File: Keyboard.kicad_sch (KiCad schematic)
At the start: 12 parts, among them J1 SPI Display, U1 MCP23017_SO, U2 MCP23017_SO, U3 Seeeduino Xiao nRF52840

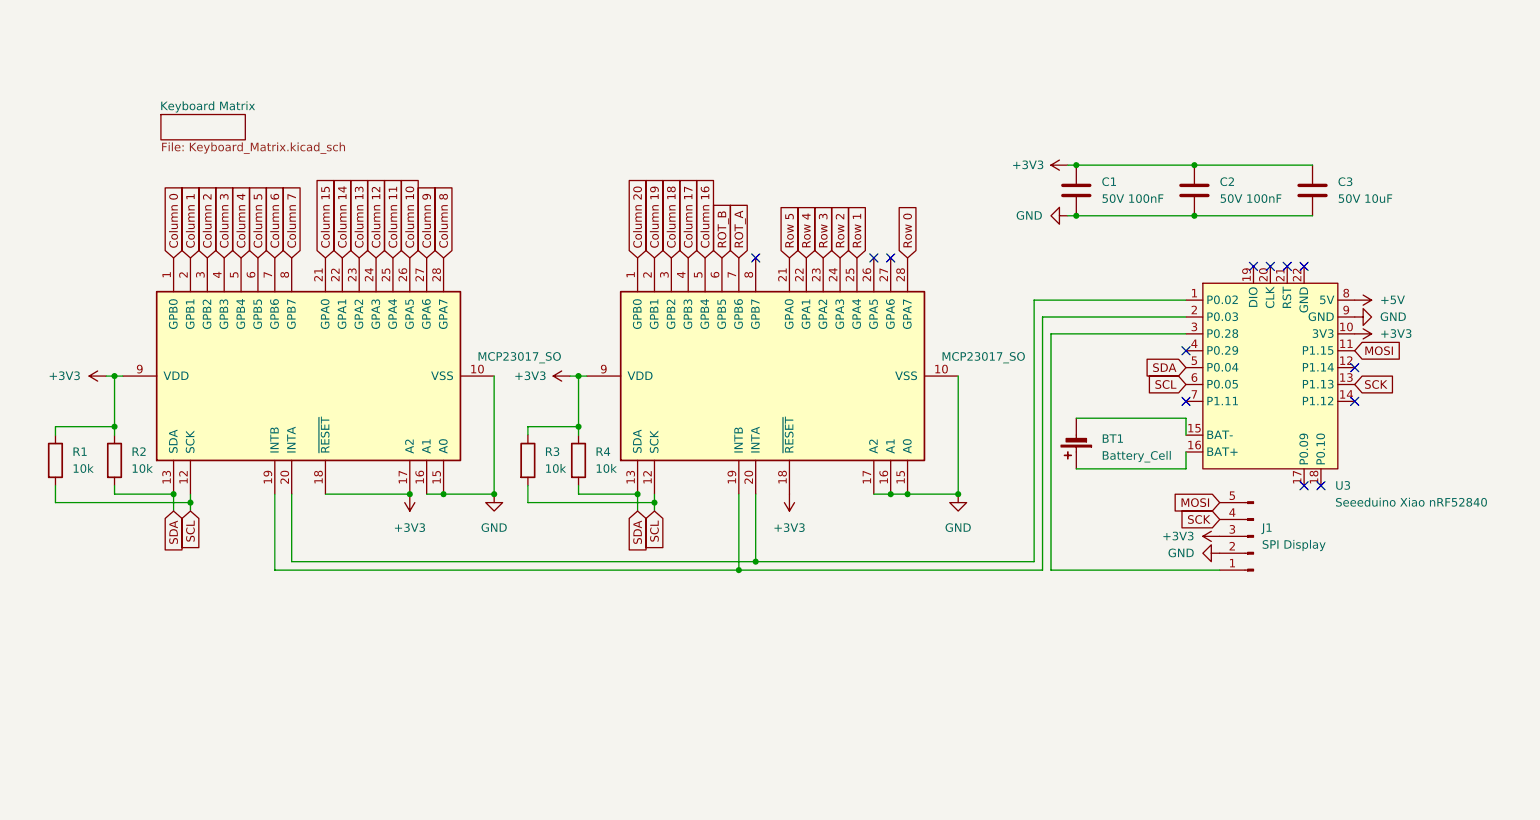
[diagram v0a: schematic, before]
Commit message: Replaced Rotary Encoder.
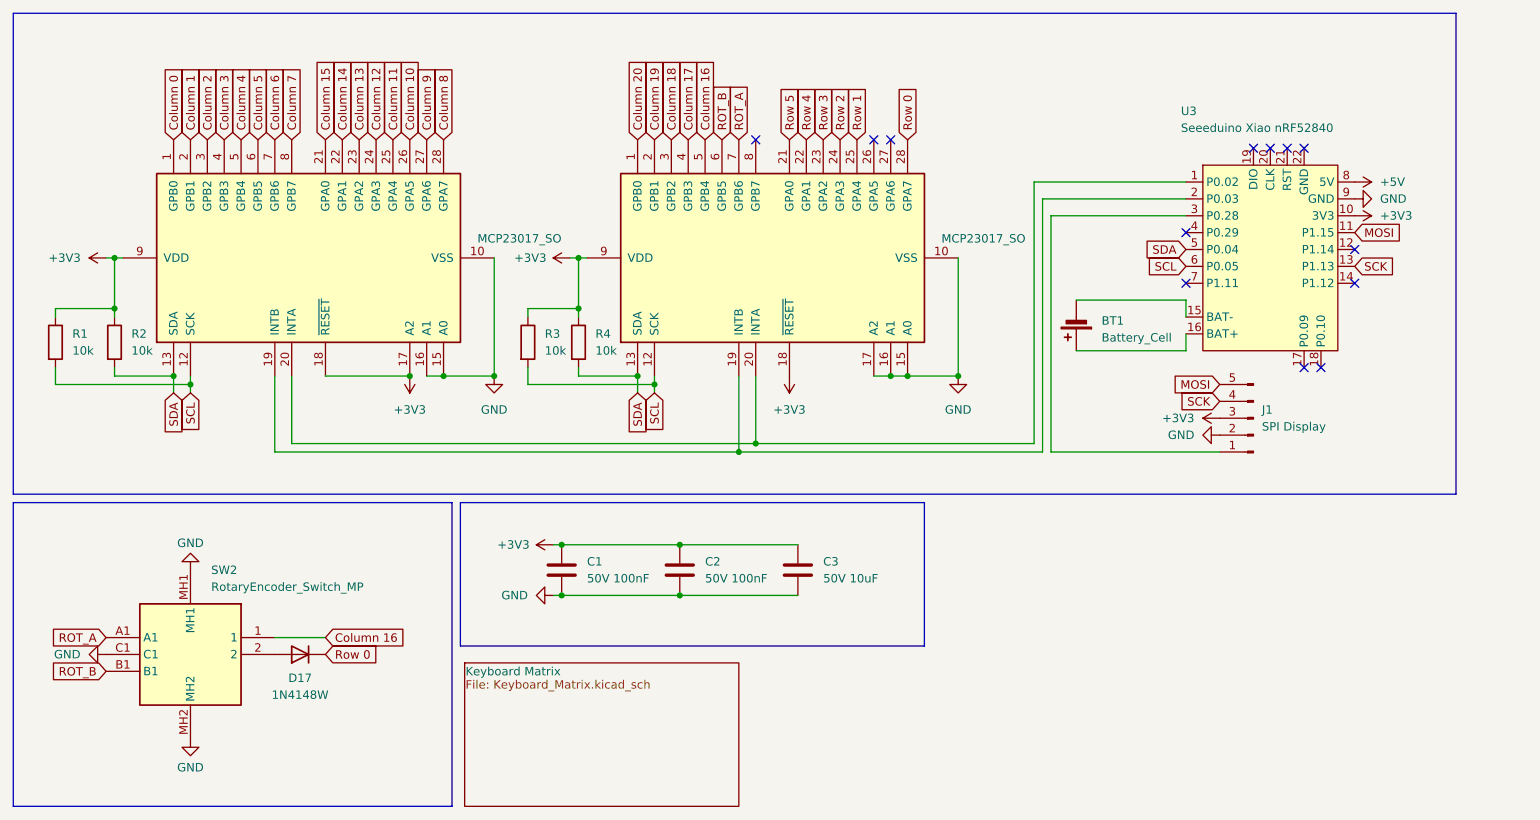
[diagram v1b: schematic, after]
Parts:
- added D17: 1N4148W, Diode_SMD:D_SOD-123, symbol Diode:1N4148W
- added SW2: RotaryEncoder_Switch_MP, SamacSys_Parts:PEC11L4115FS0020, symbol SamacSys_Parts:PEC11L-4115F-S0020
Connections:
- net Column 16: now also SW2.1
- net GND: now also SW2.C1, SW2.MH1, SW2.MH2
- net ROT_A: now also SW2.A1
- net ROT_B: now also SW2.B1
- net Row 0: now also D17.1 (K)
- new net: D17.2 (A), SW2.2
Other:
- moved on the sheet: BT1, C1, C2, C3, J1, R1, R2, R3, R4, U3

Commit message: Changed routing.
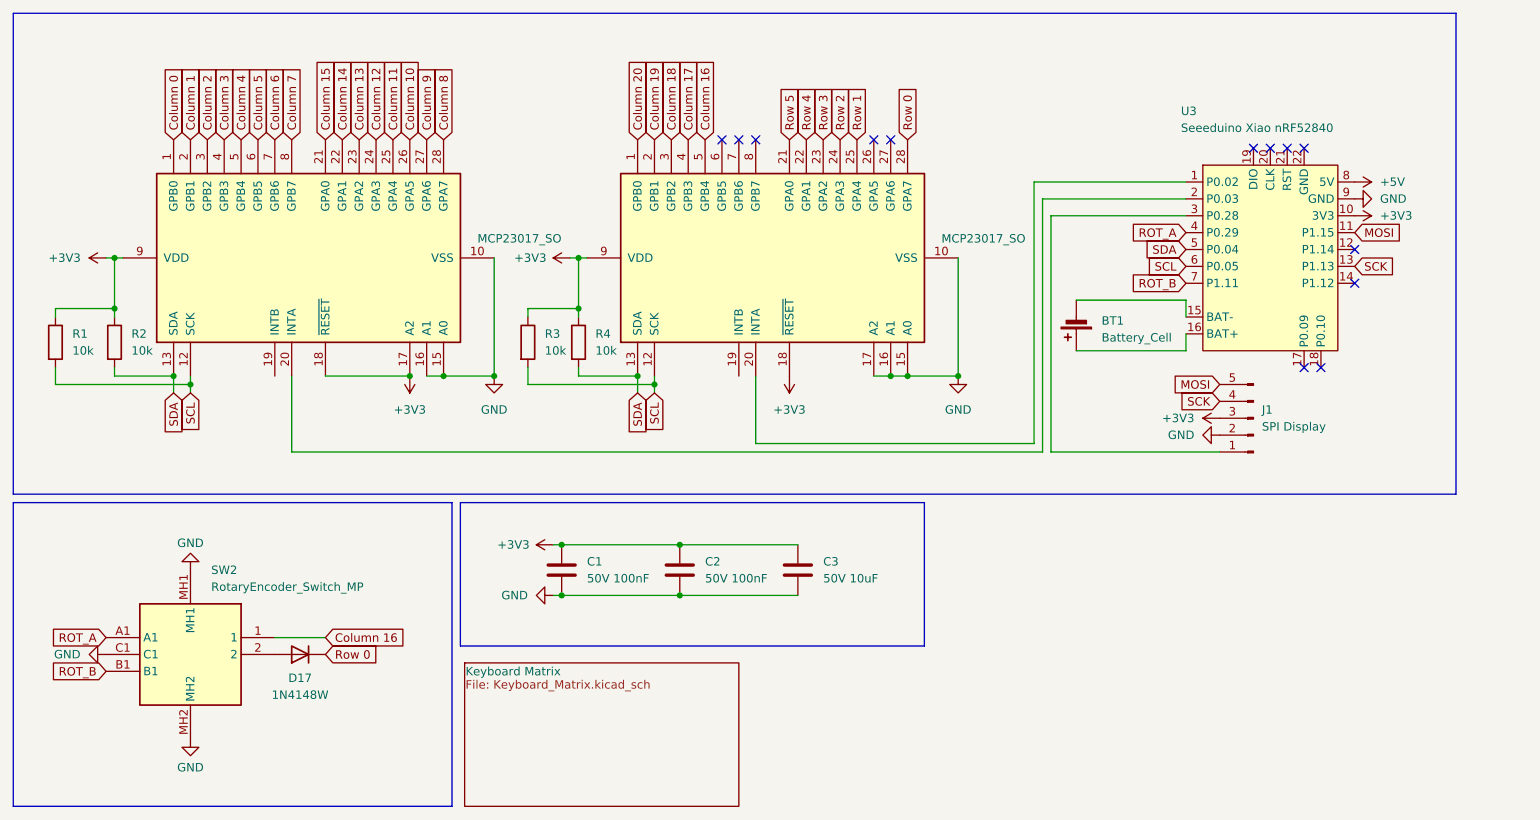
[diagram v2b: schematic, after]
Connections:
- net ROT_A: now also U3.4 (P0.29); no longer U2.7 (GPB6)
- net ROT_B: now also U3.7 (P1.11); no longer U2.6 (GPB5)
- net at U2.20 (INTA), U3.1 (P0.02): no longer U1.20 (INTA)
- new net: U1.20 (INTA), U3.2 (P0.03)
- now unconnected: U1.19 (INTB), U2.19 (INTB)
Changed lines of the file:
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@@
-	)
-	(junction
-		(at 125.73 78.74)
-		(diameter 0)
-		(color 0 0 0 0)
-	)
-	(junction
-		(at 123.19 80.01)
-		(diameter 0)
-		(color 0 0 0 0)
 	)
 	(junction
@@
 	)
 	(no_connect
-		(at 190.5 46.99)
+		(at 200.66 34.29)
 	)
 	(no_connect
-		(at 190.5 54.61)
-	)
-	(no_connect
-		(at 200.66 34.29)
+		(at 120.65 33.02)
 	)
 	(no_connect
@@
 	)
 	(no_connect
+		(at 123.19 33.02)
+	)
+	(no_connect
 		(at 203.2 34.29)
 	)
@@
 	(wire
 		(pts
-			(xy 55.88 78.74) (xy 125.73 78.74)
-		)
-		(stroke
-			(width 0)
-			(type default)
-		)
-	)
-	(wire
-		(pts
 			(xy 95.25 93.98) (xy 96.52 93.98)
 		)
@@
 	(wire
 		(pts
-			(xy 55.88 68.58) (xy 55.88 78.74)
-		)
-		(stroke
-			(width 0)
-			(type default)
-		)
-	)
-	(wire
-		(pts
 			(xy 170.18 44.45) (xy 170.18 80.01)
 		)
@@
 	(wire
 		(pts
-			(xy 123.19 68.58) (xy 123.19 80.01)
-		)
-		(stroke
-			(width 0)
-			(type default)
-		)
-	)
-	(wire
-		(pts
 			(xy 173.99 64.77) (xy 190.5 64.77)
 		)
@@
 	(wire
 		(pts
-			(xy 53.34 68.58) (xy 53.34 80.01)
-		)
-		(stroke
-			(width 0)
-			(type default)
-		)
-	)
-	(wire
-		(pts
-			(xy 123.19 80.01) (xy 168.91 80.01)
+			(xy 55.88 68.58) (xy 55.88 80.01)
 		)
 		(stroke
@@
 	(wire
 		(pts
+			(xy 55.88 80.01) (xy 168.91 80.01)
+		)
+		(stroke
+			(width 0)
+			(type default)
+		)
+	)
+	(wire
+		(pts
 			(xy 20.32 58.42) (xy 29.21 58.42)
 		)
@@
 	(wire
 		(pts
-			(xy 53.34 80.01) (xy 123.19 80.01)
-		)
-		(stroke
-			(width 0)
-			(type default)
-		)
-	)
-	(wire
-		(pts
 			(xy 170.18 80.01) (xy 195.58 80.01)
 		)
@@
 	(global_label "ROT_B"
 		(shape input)
-		(at 120.65 33.02 90)
-		(fields_autoplaced yes)
-		(effects
-			(font
-				(size 1.27 1.27)
-			)
-			(justify left)
-		)
-		(property "Intersheetrefs" "${INTERSHEET_REFS}"
-			(at 120.65 24.2291 90)
-			(effects
-				(font
-					(size 1.27 1.27)
-				)
-				(justify left)
+		(at 190.5 54.61 180)
+		(fields_autoplaced yes)
+		(effects
+			(font
+				(size 1.27 1.27)
+			)
+			(justify right)
+		)
+		(property "Intersheetrefs" "${INTERSHEET_REFS}"
+			(at 181.7091 54.61 0)
+			(effects
+				(font
+					(size 1.27 1.27)
+				)
+				(justify right)
 				(hide yes)
 			)
@@
 	(global_label "ROT_A"
 		(shape input)
-		(at 123.19 33.02 90)
-		(fields_autoplaced yes)
-		(effects
-			(font
-				(size 1.27 1.27)
-			)
-			(justify left)
-		)
-		(property "Intersheetrefs" "${INTERSHEET_REFS}"
-			(at 123.19 24.4105 90)
-			(effects
-				(font
-					(size 1.27 1.27)
-				)
-				(justify left)
-				(hide yes)
-			)
+		(at 190.5 46.99 180)
+		(fields_autoplaced yes)
+		(effects
+			(font
+				(size 1.27 1.27)
+			)
+			(justify right)
+		)
+		(property "Intersheetrefs" "${INTERSHEET_REFS}"
+			(at 181.8905 46.99 0)
+			(effects
+				(font
+					(size 1.27 1.27)
+				)
+				(justify right)
+				(hide yes)
+			)
